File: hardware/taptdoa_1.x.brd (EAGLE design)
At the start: 66 x 63.2 mm, 78 parts, among them J5 105017-0001, U1 SN74HCT245PWR, U2 AP2112K-3.3TRG1, U3 STM32F103RBT6, Y1 8MHz

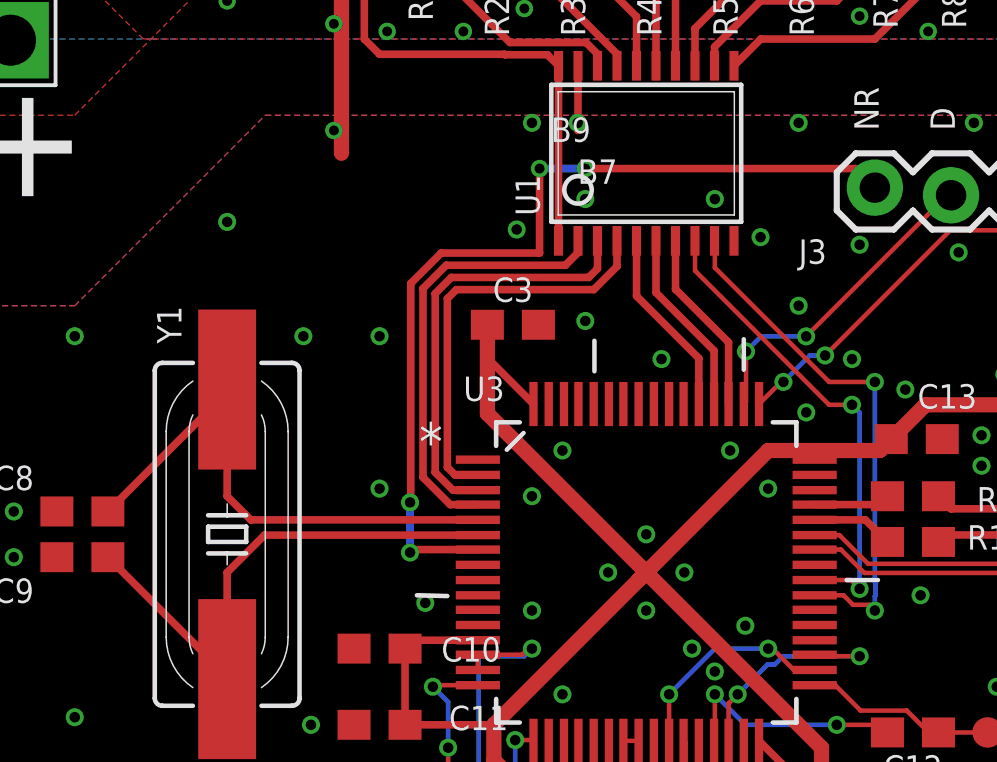
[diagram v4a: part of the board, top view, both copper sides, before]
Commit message: new board rev with leds, fix swd pins
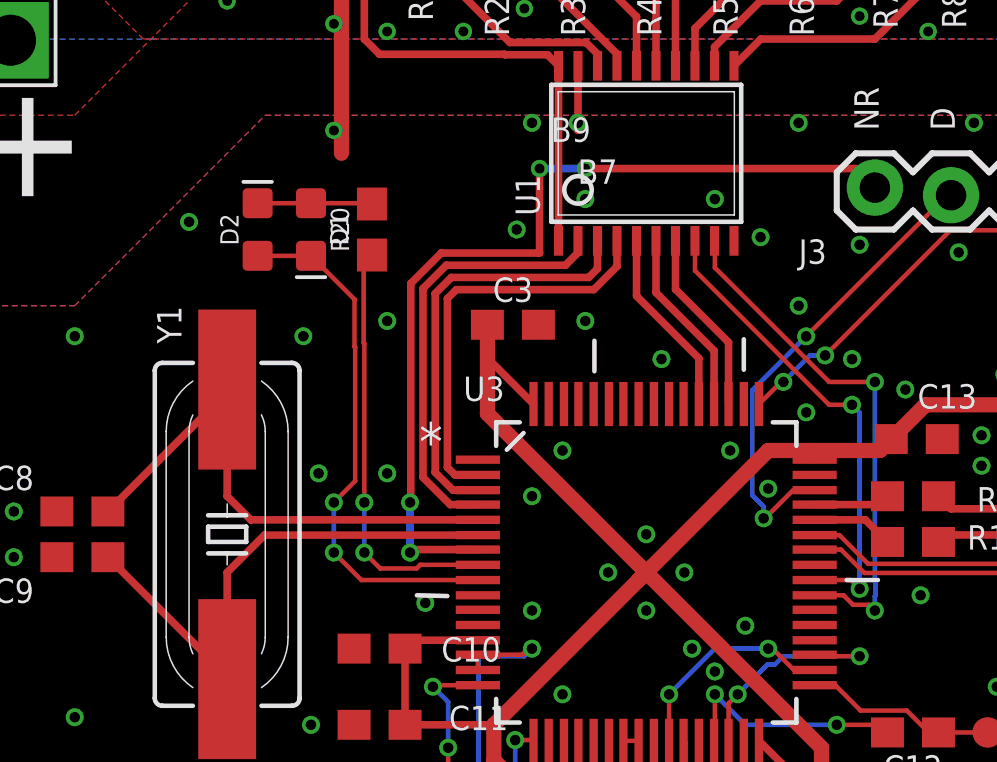
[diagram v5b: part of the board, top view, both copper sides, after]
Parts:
- added D1, D2: (no value), SparkFun-LED:LED-0603
- added R20: 75, SparkFun-Resistors:0603
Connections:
- net N$2 renamed PC8
- net N$22 renamed PC12
- net N$24 renamed PC13
- net N$25 renamed PC14
- net N$26 renamed PC15
- net N$4 renamed PC9
- net N$6 renamed PC10
- net N$8 renamed PC11
- new net N$1: R20.1, U3.8
- new net N$2: D1.A, D2.C, R20.2
- new net N$3: D1.C, D2.A, U3.9
- net PA13: now also U3.46; no longer U3.50
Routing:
- net N$3: track 0.00 -> 17.8 mm, vias 0 -> 2
- net N$1: track 0.00 -> 14.1 mm, vias 0 -> 2
- net PA13: track 10.8 -> 15.8 mm
- net N$2: track 0.00 -> 3.82 mm
- net GND: vias 222 -> 223
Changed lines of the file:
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@@
 <setting verticaltext="up"/>
 </settings>
-<grid distance="50" unitdist="mil" unit="inch" style="lines" multiple="1" display="yes" altdistance="1" altunitdist="mil" altunit="mil"/>
+<grid distance="50" unitdist="mil" unit="mil" style="lines" multiple="1" display="yes" altdistance="10" altunitdist="mil" altunit="mil"/>
 <layers>
 <layer number="1" name="Top" color="4" fill="1" visible="yes" active="yes"/>
@@
 <element name="TP12" library="SparkFun-Connectors" library_urn="urn:adsk.eagle:library:513" package="PAD.03X.04" package3d_urn="urn:adsk.eagle:package:38287/1" value="TEST-POINT3X4" x="48.3108" y="11.0998"/>
 <element name="TP13" library="SparkFun-Connectors" library_urn="urn:adsk.eagle:library:513" package="PAD.03X.04" package3d_urn="urn:adsk.eagle:package:38287/1" value="TEST-POINT3X4" x="53.7718" y="17.1196"/>
+<element name="D1" library="SparkFun-LED" library_urn="urn:adsk.eagle:library:529" package="LED-0603" package3d_urn="urn:adsk.eagle:package:39354/1" value="" x="23.114" y="38.1" rot="R270"/>
+<element name="D2" library="SparkFun-LED" library_urn="urn:adsk.eagle:library:529" package="LED-0603" package3d_urn="urn:adsk.eagle:package:39354/1" value="" x="21.336" y="38.1" rot="R90"/>
+<element name="R20" library="SparkFun-Resistors" library_urn="urn:adsk.eagle:library:532" package="0603" package3d_urn="urn:adsk.eagle:package:39650/1" value="75" x="25.146" y="38.1" rot="R90">
+<attribute name="PROD_ID" value="RES-12438" x="25.146" y="38.1" size="1.778" layer="27" rot="R90" display="off"/>
+</element>
 </elements>
 <signals>
@@
 <via x="23.114" y="21.59" extent="1-16" drill="0.35"/>
 <via x="26.924" y="25.654" extent="1-16" drill="0.35"/>
-<via x="25.4" y="29.464" extent="1-16" drill="0.35"/>
+<via x="23.368" y="29.972" extent="1-16" drill="0.35"/>
 <via x="22.86" y="34.544" extent="1-16" drill="0.35"/>
-<via x="25.4" y="34.544" extent="1-16" drill="0.35"/>
+<via x="25.654" y="35.052" extent="1-16" drill="0.35"/>
 <via x="29.972" y="38.1" extent="1-16" drill="0.35"/>
 <via x="36.576" y="39.116" extent="1-16" drill="0.35"/>
-<via x="20.32" y="38.354" extent="1-16" drill="0.35"/>
+<via x="19.05" y="38.354" extent="1-16" drill="0.35"/>
 <via x="15.24" y="34.544" extent="1-16" drill="0.35"/>
 <via x="8.89" y="34.544" extent="1-16" drill="0.35"/>
@@
 <via x="34.798" y="33.782" extent="1-16" drill="0.35"/>
 <via x="25.654" y="44.704" extent="1-16" drill="0.3302"/>
+<via x="25.654" y="29.972" extent="1-16" drill="0.35"/>
 </signal>
 <signal name="+3V3">
@@
 <signal name="PA13">
 <contactref element="J3" pad="2"/>
-<contactref element="U3" pad="50"/>
-<wire x1="37.5412" y1="32.2834" x2="37.6146" y2="32.3568" width="0.1524" layer="1"/>
-<wire x1="37.6146" y1="32.3568" x2="37.6146" y2="34.036" width="0.1524" layer="1"/>
-<via x="37.6146" y="34.036" extent="1-16" drill="0.35"/>
-<wire x1="37.6146" y1="34.036" x2="38.11679375" y2="34.53819375" width="0.1524" layer="16"/>
-<wire x1="38.11679375" y1="34.53819375" x2="39.61819375" y2="34.53819375" width="0.1524" layer="16"/>
 <via x="39.61819375" y="34.53819375" extent="1-16" drill="0.35"/>
 <wire x1="39.61819375" y1="34.53819375" x2="44.323" y2="39.243" width="0.1524" layer="1"/>
 <wire x1="44.323" y1="39.243" x2="44.45" y2="39.243" width="0.1524" layer="1"/>
+<contactref element="U3" pad="46"/>
+<via x="38.2016" y="28.4734" extent="1-16" drill="0.35"/>
+<wire x1="38.2016" y1="28.8660125" x2="38.2016" y2="28.4734" width="0.1524" layer="16"/>
+<wire x1="37.8234" y1="29.2442125" x2="38.2016" y2="28.8660125" width="0.1524" layer="16"/>
+<wire x1="37.8234" y1="32.7434" x2="37.8234" y2="29.2442125" width="0.1524" layer="16"/>
+<wire x1="39.61819375" y1="34.53819375" x2="37.8234" y2="32.7434" width="0.1524" layer="16"/>
+<wire x1="39.1737125" y1="29.4005" x2="39.8907" y2="29.4005" width="0.1524" layer="1"/>
+<wire x1="39.8907" y1="29.4005" x2="39.9034" y2="29.4132" width="0.1524" layer="1"/>
+<wire x1="38.2016" y1="28.4734" x2="38.2466125" y2="28.4734" width="0.1524" layer="1"/>
+<wire x1="38.2466125" y1="28.4734" x2="39.1737125" y2="29.4005" width="0.1524" layer="1"/>
 </signal>
 <signal name="PA14">
@@
 <wire x1="50.38" y1="49.11" x2="44.45" y2="49.11" width="0.1524" layer="1"/>
 </signal>
-<signal name="N$2">
+<signal name="PC8">
 <contactref element="U1" pad="9"/>
 <contactref element="U3" pad="39"/>
@@
 <wire x1="41.1822125" y1="25.5914" x2="40.8656125" y2="25.908" width="0.1524" layer="1"/>
 </signal>
-<signal name="N$4">
+<signal name="PC9">
 <contactref element="U1" pad="8"/>
 <contactref element="U3" pad="40"/>
@@
 <wire x1="35.915" y1="36.729" x2="40.386" y2="32.258" width="0.1524" layer="1"/>
 </signal>
-<signal name="N$6">
+<signal name="PC10">
 <contactref element="U3" pad="51"/>
 <contactref element="U1" pad="7"/>
@@
 <wire x1="37.0332" y1="34.3408" x2="35.265" y2="36.109" width="0.254" layer="1"/>
 </signal>
-<signal name="N$8">
+<signal name="PC11">
 <contactref element="U1" pad="6"/>
 <contactref element="U3" pad="52"/>
@@
 <wire x1="36.5506" y1="34.0614" x2="34.615" y2="35.997" width="0.254" layer="1"/>
 </signal>
-<signal name="N$22">
+<signal name="PC12">
 <contactref element="U3" pad="53"/>
 <contactref element="U1" pad="5"/>
@@
 <wire x1="36.0426" y1="33.8074" x2="33.965" y2="35.885" width="0.254" layer="1"/>
 </signal>
-<signal name="N$24">
+<signal name="PC13">
 <contactref element="U1" pad="4"/>
 <contactref element="U3" pad="2"/>
@@
 <wire x1="28.6766" y1="29.9212" x2="27.91316875" y2="29.9212" width="0.254" layer="1"/>
 </signal>
-<signal name="N$25">
+<signal name="PC14">
 <contactref element="U3" pad="3"/>
 <contactref element="U1" pad="3"/>
@@
 <wire x1="28.6766" y1="29.4132" x2="27.84643125" y2="29.4132" width="0.254" layer="1"/>
 </signal>
-<signal name="N$26">
+<signal name="PC15">
 <contactref element="U1" pad="2"/>
 <contactref element="U3" pad="4"/>
@@
 <wire x1="5.93" y1="10.58" x2="3.81" y2="12.7" width="0.254" layer="1"/>
 </signal>
+<signal name="N$1">
+<contactref element="U3" pad="8"/>
+<contactref element="R20" pad="1"/>
+<via x="24.892" y="27.3332" extent="1-16" drill="0.35"/>
+<wire x1="28.6766" y1="26.924" x2="26.7571875" y2="26.924" width="0.1524" layer="1"/>
+<wire x1="26.7571875" y1="26.924" x2="26.6357875" y2="26.8026" width="0.1524" layer="1"/>
+<wire x1="26.6357875" y1="26.8026" x2="25.4226" y2="26.8026" width="0.1524" layer="1"/>
+<wire x1="25.4226" y1="26.8026" x2="24.892" y2="27.3332" width="0.1524" layer="1"/>
+<wire x1="24.892" y1="27.3332" x2="24.892" y2="29.004" width="0.1524" layer="16"/>
+<via x="24.892" y="29.004" extent="1-16" drill="0.35"/>
+<wire x1="24.892" y1="29.004" x2="24.892" y2="34.3016125" width="0.1524" layer="1"/>
+<wire x1="24.892" y1="34.3016125" x2="24.8694" y2="34.3242125" width="0.1524" layer="1"/>
+<wire x1="24.8694" y1="34.3242125" x2="24.8694" y2="36.9734" width="0.1524" layer="1"/>
+<wire x1="24.8694" y1="36.9734" x2="25.146" y2="37.25" width="0.1524" layer="1"/>
+</signal>
+<signal name="N$2">
+<contactref element="R20" pad="2"/>
+<contactref element="D1" pad="A"/>
+<contactref element="D2" pad="C"/>
+<wire x1="21.336" y1="38.977" x2="23.114" y2="38.977" width="0.1524" layer="1"/>
+<wire x1="23.114" y1="38.977" x2="25.119" y2="38.977" width="0.1524" layer="1"/>
+<wire x1="25.119" y1="38.977" x2="25.146" y2="38.95" width="0.1524" layer="1"/>
+</signal>
+<signal name="N$3">
+<contactref element="D2" pad="A"/>
+<contactref element="D1" pad="C"/>
+<contactref element="U3" pad="9"/>
+<wire x1="21.336" y1="37.223" x2="23.114" y2="37.223" width="0.1524" layer="1"/>
+<wire x1="28.6766" y1="26.416" x2="24.7932" y2="26.416" width="0.1524" layer="1"/>
+<wire x1="24.7932" y1="26.416" x2="23.876" y2="27.3332" width="0.1524" layer="1"/>
+<via x="23.876" y="27.3332" extent="1-16" drill="0.35"/>
+<wire x1="23.876" y1="27.3332" x2="23.876" y2="29.004" width="0.1524" layer="16"/>
+<via x="23.876" y="29.004" extent="1-16" drill="0.35"/>
+<wire x1="23.876" y1="29.004" x2="24.5872" y2="29.7152" width="0.1524" layer="1"/>
+<wire x1="24.5872" y1="34.17535625" x2="24.5646" y2="34.19795625" width="0.1524" layer="1"/>
+<wire x1="24.5646" y1="35.7724" x2="23.114" y2="37.223" width="0.1524" layer="1"/>
+<wire x1="24.5646" y1="34.19795625" x2="24.5646" y2="35.7724" width="0.1524" layer="1"/>
+<wire x1="24.5872" y1="29.7152" x2="24.5872" y2="34.17535625" width="0.1524" layer="1"/>
+</signal>
 </signals>

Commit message: more LEDs
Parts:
- added D3, D4, D5, D6: (no value), SparkFun-LED:LED-0603
- added R21, R22, R23, R24: 10k, SparkFun-Resistors:0603
- added R25, R26: 33, SparkFun-Resistors:0603
- R20: value 75 -> 33
- U3: value STM32F103RBT6 -> STM32F303RET6
- moved D1 20.7 mm to (5.08, 27.9), turned to 0 degrees
- moved R20 18.4 mm to (10.2, 27.4), turned to 180 degrees
- moved D2 12.5 mm to (14.0, 27.9), turned to 180 degrees
- moved C8 1.80 mm to (16.8, 30.0), turned to 270 degrees
- moved C9 1.80 mm to (16.8, 25.9), turned to 270 degrees
- moved J4 1.27 mm to (54.1, 24.6)
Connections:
- removed net N$3: D1.C, D2.A, U3.9
- new net N$22: D3.C, D4.A, D5.C, D6.A, R25.2
- new net N$4: R25.1, U3.10
- new net N$5: R26.1, U3.9
- new net N$6: D1.C, D2.A, D3.A, D4.C, R26.2
- net +3V3: now also R21.2, R22.2, R23.2, R24.2
- net N$19: now also R22.1
- net N$2: now also D5.A, D6.C
- net N$20: now also R24.1
- net N$21: now also R21.1
- net N$23: now also R23.1
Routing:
- net +3V3: track 85.7 -> 119.2 mm
- net N$6: track 0.00 -> 29.6 mm
- net N$22: track 0.00 -> 27.6 mm, vias 0 -> 2
- net N$2: track 3.82 -> 30.3 mm
- net N$4: track 0.00 -> 18.5 mm, vias 0 -> 2
- net N$5: track 0.00 -> 17.9 mm, vias 0 -> 2
- net N$3: track 17.8 -> 0.00 mm, vias 2 -> 0
- net N$21: track 3.84 -> 13.9 mm, vias 0 -> 2
- net N$20: track 4.19 -> 13.9 mm, vias 0 -> 2
- net N$23: track 4.19 -> 10.8 mm
- net N$1: track 14.1 -> 18.2 mm
- net N$19: track 3.84 -> 7.84 mm
- net PD0_OSC_IN: track 17.9 -> 16.4 mm
- net PD1_OSC_OUT: track 18.1 -> 16.6 mm
- net UART1_TX: track 12.0 -> 10.8 mm
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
